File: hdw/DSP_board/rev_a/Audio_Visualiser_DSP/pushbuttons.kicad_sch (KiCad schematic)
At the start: 41 parts, among them J1901 Power Button, J1902 Power, SW1901 Cap_Touch, SW1902 RotaryEncoder_Switch, SW1903 Power, U1901 AT42QT1010-TSHR, U1902 74LVC1G97, U1903 74LVC1G97, U1904 74LVC1G97, U1905 74LVC1G97, U1906 74LVC1G97, U1907 74LVC1G79

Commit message: cleared stale digikey part numbers
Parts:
- C1901, C1903, C1904, C1905, C1906, C1907, C1908, C1909, C1910, C1912, C1913: Digi-Key PN 490-10697-1-ND -> (none)
- C1902: Digi-Key PN 445-12201-1-ND -> (none)
- C1911: Digi-Key PN 490-GRM155R61A106ME11DCT-ND -> (none)
- R1901, R1902: Digi-Key PN RMCF0402FT1K00CT-ND -> (none)
- R1903, R1904, R1906, R1907, R1908, R1909, R1910, R1911, R1912, R1913, R1915, R1916: Digi-Key PN RMCF0402FT10K0CT-ND -> (none)
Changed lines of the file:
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@@
 			)
 		)
-		(property "Digi-Key PN" "490-10697-1-ND"
+		(property "Digi-Key PN" ""
 			(at 55.245 160.02 0)
 			(hide yes)
@@
 			)
 		)
-		(property "Digi-Key PN" "490-GRM155R61A106ME11DCT-ND"
+		(property "Digi-Key PN" ""
 			(at 147.955 36.83 0)
 			(hide yes)
@@
 			)
 		)
-		(property "Digi-Key PN" "RMCF0402FT1K00CT-ND"
+		(property "Digi-Key PN" ""
 			(at 44.45 29.21 0)
 			(hide yes)
@@
 			)
 		)
-		(property "Digi-Key PN" "490-10697-1-ND"
+		(property "Digi-Key PN" ""
 			(at 83.185 74.93 0)
 			(hide yes)
@@
 			)
 		)
-		(property "Digi-Key PN" "490-10697-1-ND"
+		(property "Digi-Key PN" ""
 			(at 83.185 111.76 0)
 			(hide yes)
@@
 			)
 		)
-		(property "Digi-Key PN" "RMCF0402FT1K00CT-ND"
+		(property "Digi-Key PN" ""
 			(at 44.45 34.29 0)
 			(hide yes)
@@
 			)
 		)
-		(property "Digi-Key PN" "490-10697-1-ND"
+		(property "Digi-Key PN" ""
 			(at 103.505 142.24 0)
 			(hide yes)
@@
 			)
 		)
-		(property "Digi-Key PN" "RMCF0402FT10K0CT-ND"
+		(property "Digi-Key PN" ""
 			(at 101.6 64.77 0)
 			(hide yes)
@@
 			)
 		)
-		(property "Digi-Key PN" "490-10697-1-ND"
+		(property "Digi-Key PN" ""
 			(at 159.385 143.51 0)
 			(hide yes)
@@
 			)
 		)
-		(property "Digi-Key PN" "RMCF0402FT10K0CT-ND"
+		(property "Digi-Key PN" ""
 			(at 195.58 139.7 0)
 			(hide yes)
@@
 			)
 		)
-		(property "Digi-Key PN" "490-10697-1-ND"
+		(property "Digi-Key PN" ""
 			(at 103.505 165.1 0)
 			(hide yes)
@@
 			)
 		)
-		(property "Digi-Key PN" "490-10697-1-ND"
+		(property "Digi-Key PN" ""
 			(at 71.755 160.02 0)
 			(hide yes)
@@
 			)
 		)
-		(property "Digi-Key PN" "RMCF0402FT10K0CT-ND"
+		(property "Digi-Key PN" ""
 			(at 130.81 41.91 0)
 			(hide yes)
@@
 			)
 		)
-		(property "Digi-Key PN" "RMCF0402FT10K0CT-ND"
+		(property "Digi-Key PN" ""
 			(at 73.66 127 0)
 			(hide yes)
@@
 			)
 		)
-		(property "Digi-Key PN" "RMCF0402FT10K0CT-ND"
+		(property "Digi-Key PN" ""
 			(at 152.4 114.3 0)
 			(hide yes)
@@
 			)
 		)
-		(property "Digi-Key PN" "RMCF0402FT10K0CT-ND"
+		(property "Digi-Key PN" ""
 			(at 175.26 38.1 0)
 			(hide yes)
@@
 			)
 		)
-		(property "Digi-Key PN" "445-12201-1-ND"
+		(property "Digi-Key PN" ""
 			(at 18.542 163.576 0)
 			(hide yes)
@@
 			)
 		)
-		(property "Digi-Key PN" "490-10697-1-ND"
+		(property "Digi-Key PN" ""
 			(at 120.015 116.84 0)
 			(hide yes)
@@
 			)
 		)
-		(property "Digi-Key PN" "490-10697-1-ND"
+		(property "Digi-Key PN" ""
 			(at 145.415 43.18 0)
 			(hide yes)
@@
 			)
 		)
-		(property "Digi-Key PN" "RMCF0402FT10K0CT-ND"
+		(property "Digi-Key PN" ""
 			(at 135.89 139.7 0)
 			(hide yes)
@@
 			)
 		)
-		(property "Digi-Key PN" "RMCF0402FT10K0CT-ND"
+		(property "Digi-Key PN" ""
 			(at 152.4 77.47 0)
 			(hide yes)
@@
 			)
 		)
-		(property "Digi-Key PN" "490-10697-1-ND"
+		(property "Digi-Key PN" ""
 			(at 120.015 80.01 0)
 			(hide yes)
@@
 			)
 		)
-		(property "Digi-Key PN" "RMCF0402FT10K0CT-ND"
+		(property "Digi-Key PN" ""
 			(at 135.89 162.56 0)
 			(hide yes)
@@
 			)
 		)
-		(property "Digi-Key PN" "RMCF0402FT10K0CT-ND"
+		(property "Digi-Key PN" ""
 			(at 90.17 127 0)
 			(hide yes)
@@
 			)
 		)
-		(property "Digi-Key PN" "RMCF0402FT10K0CT-ND"
+		(property "Digi-Key PN" ""
 			(at 101.6 101.6 0)
 			(hide yes)
@@
 			)
 		)
-		(property "Digi-Key PN" "490-10697-1-ND"
+		(property "Digi-Key PN" ""
 			(at 74.295 44.45 0)
 			(hide yes)
@@
 			)
 		)
-		(property "Digi-Key PN" "RMCF0402FT10K0CT-ND"
+		(property "Digi-Key PN" ""
 			(at 123.19 39.37 0)
 			(hide yes)

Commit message: updated rca jack
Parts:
- J1901: footprint (none) -> Button_Switch_THT:SW_PUSH_6mm
- SW1901: now left out of the parts list
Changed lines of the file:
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@@
 		(body_style 1)
 		(exclude_from_sim yes)
-		(in_bom yes)
+		(in_bom no)
 		(on_board yes)
 		(in_pos_files yes)
@@
 			)
 		)
-		(property "Footprint" ""
+		(property "Footprint" "Button_Switch_THT:SW_PUSH_6mm"
 			(at 38.1 24.13 0)
 			(hide yes)

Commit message: assigned some footprints
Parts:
- U1907: footprint (none) -> Package_TO_SOT_SMD:SOT-363_SC-70-6

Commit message: assigned many digi-key part numbers
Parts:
- C1901, C1903, C1905, C1906: Dielectric X7R -> X7S; Digi-Key PN (none) -> 445-9116-1-ND
- C1902: Dielectric X5R -> X7R; Digi-Key PN (none) -> 490-4516-1-ND
- C1904, C1912: Digi-Key PN (none) -> 490-11917-1-ND
- C1907, C1908, C1909, C1910, C1913: Digi-Key PN (none) -> 1276-CL05B104KB5NNNCCT-ND
- C1911: Digi-Key PN (none) -> 1276-CL05A106MP6NUN8CT-ND
- J1902: Digi-Key PN (none) -> 277-1247-ND
- R1901, R1902: Digi-Key PN (none) -> 311-1.00KLRCT-ND
- R1903, R1904, R1906, R1907, R1908, R1909, R1910, R1911, R1912, R1913, R1915, R1916: Digi-Key PN (none) -> 311-10.0KLRCT-ND
- R1905, R1914: Digi-Key PN (none) -> 311-0.0LRCT-ND
- SW1903: footprint (none) -> Button_Switch_THT:SW_PUSH_6mm; Digi-Key PN (none) -> 450-1650-ND
- U1907: footprint Package_TO_SOT_SMD:SOT-363_SC-70-6 -> Package_TO_SOT_SMD:SOT-353_SC-70-5; Digi-Key PN (none) -> 296-9850-1-ND
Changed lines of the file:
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@@
 			)
 		)
-		(property "Digi-Key PN" ""
+		(property "Digi-Key PN" "445-9116-1-ND"
 			(at 55.245 160.02 0)
 			(hide yes)
@@
 			)
 		)
-		(property "Dielectric" "X7R"
+		(property "Dielectric" "X7S"
 			(at 69.85 175.26 0)
 			(show_name no)
@@
 			)
 		)
-		(property "Digi-Key PN" ""
+		(property "Digi-Key PN" "1276-CL05A106MP6NUN8CT-ND"
 			(at 147.955 36.83 0)
 			(hide yes)
@@
 			)
 		)
-		(property "Digi-Key PN" ""
+		(property "Digi-Key PN" "311-1.00KLRCT-ND"
 			(at 44.45 29.21 0)
 			(hide yes)
@@
 			)
 		)
-		(property "Digi-Key PN" ""
+		(property "Digi-Key PN" "445-9116-1-ND"
 			(at 83.185 74.93 0)
 			(hide yes)
@@
 			)
 		)
-		(property "Dielectric" "X7R"
+		(property "Dielectric" "X7S"
 			(at 97.79 90.17 0)
 			(show_name no)
@@
 			)
 		)
-		(property "Digi-Key PN" ""
+		(property "Digi-Key PN" "445-9116-1-ND"
 			(at 83.185 111.76 0)
 			(hide yes)
@@
 			)
 		)
-		(property "Dielectric" "X7R"
+		(property "Dielectric" "X7S"
 			(at 97.79 127 0)
 			(show_name no)
@@
 			)
 		)
-		(property "Digi-Key PN" ""
+		(property "Digi-Key PN" "311-1.00KLRCT-ND"
 			(at 44.45 34.29 0)
 			(hide yes)
@@
 			)
 		)
-		(property "Digi-Key PN" ""
+		(property "Digi-Key PN" "1276-CL05B104KB5NNNCCT-ND"
 			(at 103.505 142.24 0)
 			(hide yes)
@@
 			)
 		)
-		(property "Digi-Key PN" ""
+		(property "Digi-Key PN" "311-10.0KLRCT-ND"
 			(at 101.6 64.77 0)
 			(hide yes)
@@
 			)
 		)
-		(property "Digi-Key PN" ""
+		(property "Digi-Key PN" "1276-CL05B104KB5NNNCCT-ND"
 			(at 159.385 143.51 0)
 			(hide yes)
@@
 			)
 		)
-		(property "Digi-Key PN" ""
+		(property "Digi-Key PN" "311-10.0KLRCT-ND"
 			(at 195.58 139.7 0)
 			(hide yes)
@@
 			)
 		)
-		(property "Digi-Key PN" ""
+		(property "Digi-Key PN" "1276-CL05B104KB5NNNCCT-ND"
 			(at 103.505 165.1 0)
 			(hide yes)
@@
 			)
 		)
-		(property "Digi-Key PN" ""
+		(property "Digi-Key PN" "445-9116-1-ND"
 			(at 71.755 160.02 0)
 			(hide yes)
@@
 			)
 		)
-		(property "Dielectric" "X7R"
+		(property "Dielectric" "X7S"
 			(at 86.36 175.26 0)
 			(show_name no)
@@
 			)
 		)
-		(property "Digi-Key PN" ""
+		(property "Digi-Key PN" "311-10.0KLRCT-ND"
 			(at 130.81 41.91 0)
 			(hide yes)
@@
 			)
 		)
-		(property "Digi-Key PN" ""
+		(property "Digi-Key PN" "311-10.0KLRCT-ND"
 			(at 73.66 127 0)
 			(hide yes)
@@
 			)
 		)
-		(property "Digi-Key PN" ""
+		(property "Digi-Key PN" "311-0.0LRCT-ND"
 			(at 83.82 16.51 0)
 			(hide yes)
@@
 			)
 		)
-		(property "Footprint" ""
+		(property "Footprint" "Button_Switch_THT:SW_PUSH_6mm"
 			(at 72.39 88.9 0)
 			(hide yes)
@@
 			)
 		)
+		(property "Digi-Key PN" "450-1650-ND"
+			(at 77.47 88.9 0)
+			(hide yes)
+			(show_name no)
+			(do_not_autoplace no)
+			(effects
+				(font
+					(size 1.27 1.27)
+				)
+			)
+		)
 		(pin "1"
 		)
@@
 			)
 		)
-		(property "Digi-Key PN" ""
+		(property "Digi-Key PN" "311-10.0KLRCT-ND"
 			(at 152.4 114.3 0)
 			(hide yes)
@@
 			)
 		)
-		(property "Digi-Key PN" ""
+		(property "Digi-Key PN" "311-10.0KLRCT-ND"
 			(at 175.26 38.1 0)
 			(hide yes)
@@
 			)
 		)
-		(property "Digi-Key PN" ""
+		(property "Digi-Key PN" "490-4516-1-ND"
 			(at 18.542 163.576 0)
 			(hide yes)
@@
 			)
 		)
-		(property "Dielectric" "X5R"
+		(property "Dielectric" "X7R"
 			(at 74.93 45.974 90)
 			(show_name no)
@@
 			)
 		)
-		(property "Digi-Key PN" ""
+		(property "Digi-Key PN" "1276-CL05B104KB5NNNCCT-ND"
 			(at 120.015 116.84 0)
 			(hide yes)
@@
 			)
 		)
-		(property "Digi-Key PN" ""
+		(property "Digi-Key PN" "490-11917-1-ND"
 			(at 145.415 43.18 0)
 			(hide yes)
@@
 			)
 		)
+		(property "Digi-Key PN" "277-1247-ND"
+			(at 38.1 81.28 0)
+			(hide yes)
+			(show_name no)
+			(do_not_autoplace no)
+			(effects
+				(font
+					(size 1.27 1.27)
+				)
+			)
+		)
 		(pin "1"
 		)
@@
 			)
 		)
-		(property "Digi-Key PN" ""
+		(property "Digi-Key PN" "311-10.0KLRCT-ND"
 			(at 135.89 139.7 0)
 			(hide yes)
@@
 			)
 		)
-		(property "Digi-Key PN" ""
+		(property "Digi-Key PN" "311-10.0KLRCT-ND"
 			(at 152.4 77.47 0)
 			(hide yes)
@@
 			)
 		)
-		(property "Digi-Key PN" ""
+		(property "Digi-Key PN" "311-0.0LRCT-ND"
 			(at 147.32 73.66 0)
 			(hide yes)
@@
 			)
 		)
-		(property "Digi-Key PN" ""
+		(property "Digi-Key PN" "1276-CL05B104KB5NNNCCT-ND"
 			(at 120.015 80.01 0)
 			(hide yes)
@@
 			)
 		)
-		(property "Digi-Key PN" ""
+		(property "Digi-Key PN" "311-10.0KLRCT-ND"
 			(at 135.89 162.56 0)
 			(hide yes)
@@
 			)
 		)
-		(property "Footprint" "Package_TO_SOT_SMD:SOT-363_SC-70-6"
+		(property "Footprint" "Package_TO_SOT_SMD:SOT-353_SC-70-5"
 			(at 158.75 146.05 0)
 			(hide yes)
@@
 			)
 		)
+		(property "Digi-Key PN" "296-9850-1-ND"
+			(at 158.75 146.05 0)
+			(hide yes)
+			(show_name no)
+			(do_not_autoplace no)
+			(effects
+				(font
+					(size 1.27 1.27)
+				)
+			)
+		)
 		(pin "3"
 		)
@@
 			)
 		)
-		(property "Digi-Key PN" ""
+		(property "Digi-Key PN" "311-10.0KLRCT-ND"
 			(at 90.17 127 0)
 			(hide yes)
@@
 			)
 		)
-		(property "Digi-Key PN" ""
+		(property "Digi-Key PN" "311-10.0KLRCT-ND"
 			(at 101.6 101.6 0)
 			(hide yes)
@@
 			)
 		)
-		(property "Digi-Key PN" ""
+		(property "Digi-Key PN" "490-11917-1-ND"
 			(at 74.295 44.45 0)
 			(hide yes)
@@
 			)
 		)
-		(property "Digi-Key PN" ""
+		(property "Digi-Key PN" "311-10.0KLRCT-ND"
 			(at 123.19 39.37 0)
 			(hide yes)

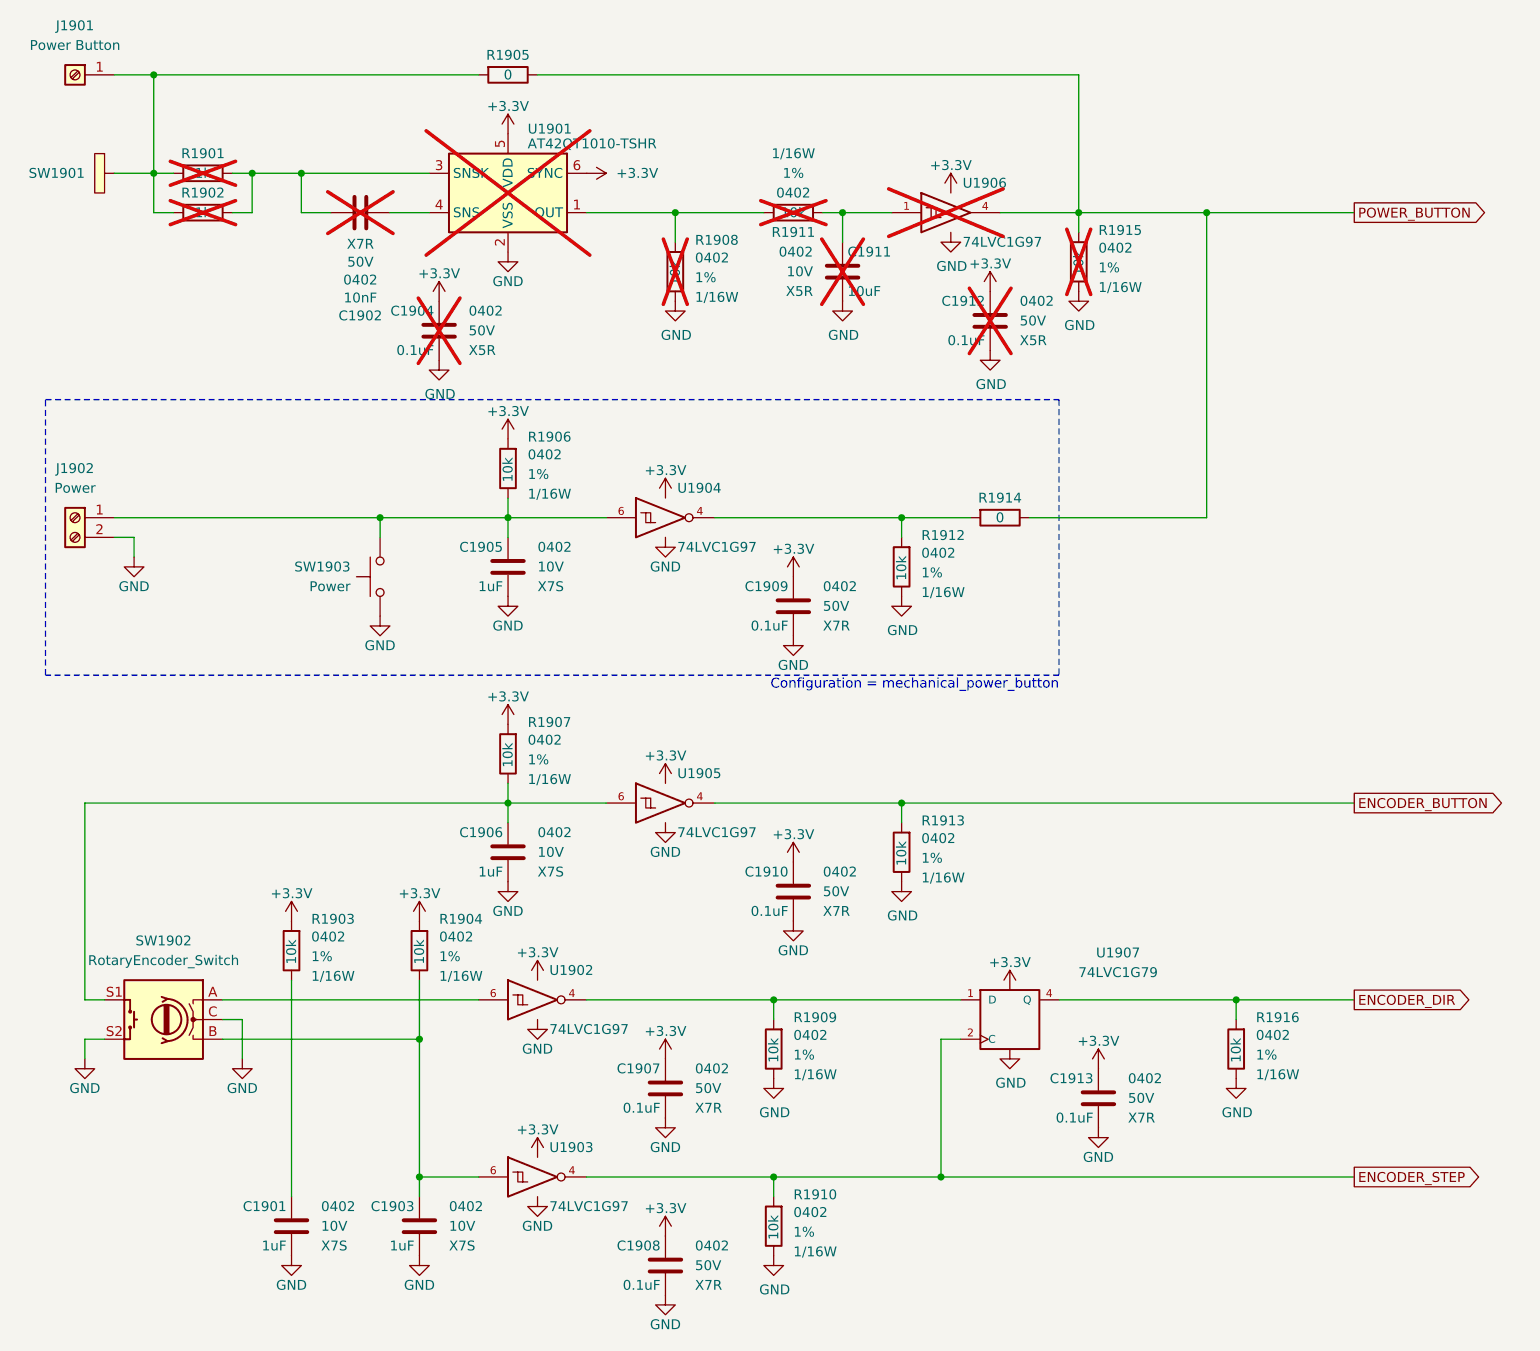
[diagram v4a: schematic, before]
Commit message: Added a bunch of stuff to the schematic
Moved to adafruit I2C rotary encoder module. Added signal test points. Added some design schematic notes. Added LEd output connector ESD diodes. Consolidated on a single schottky diode. Connected most signals to MCU
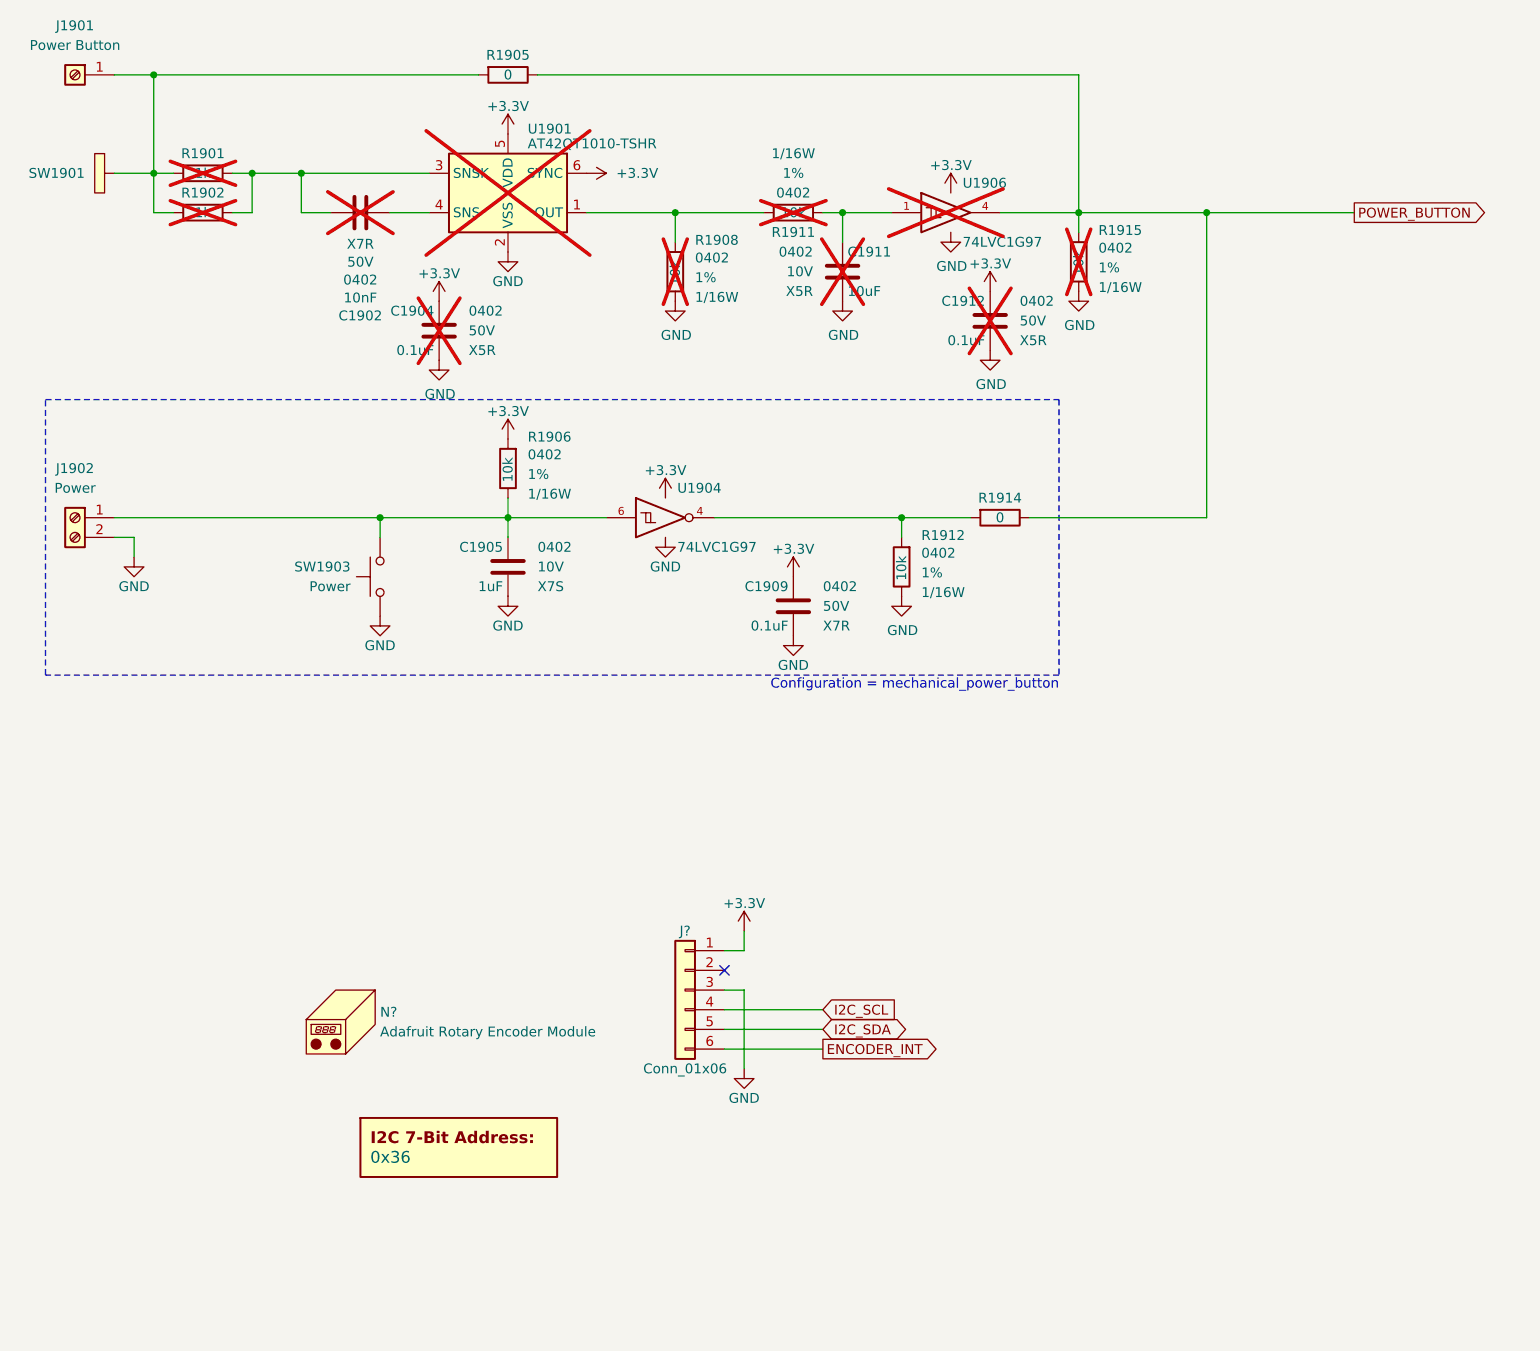
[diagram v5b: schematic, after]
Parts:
- removed C1901, C1903, C1906: 1uF, Capacitors_SMD:C_0402, symbol Custom_Library:C_Custom
- removed C1907, C1908, C1910, C1913: 0.1uF, Capacitors_SMD:C_0402, symbol Custom_Library:C_Custom
- removed R1903, R1904, R1907, R1909, R1910, R1913, R1916: 10k, Resistors_SMD:R_0402, symbol Custom_Library:R_Custom
- removed SW1902: RotaryEncoder_Switch, symbol Device:RotaryEncoder_Switch
- removed U1902, U1903, U1905: 74LVC1G97, Package_TO_SOT_SMD:SOT-363_SC-70-6, symbol Custom Library:74LVC1G97_Power_NOT
- removed U1907: 74LVC1G79, Package_TO_SOT_SMD:SOT-353_SC-70-5, symbol Custom Library:74LVC1G79_Power
- added DOC?: 0x36, symbol Custom Library:I2C_Address
- added J?: Conn_01x06, symbol Connector_Generic:Conn_01x06
- added N?: Adafruit Rotary Encoder Module, symbol Mechanical:Housing
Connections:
- net +3.3V: now also J?.1 (Pin_1)
- net GND: now also J?.3 (Pin_3)
- new net ENCODER_INT: J?.6 (Pin_6)
- new net I2C_SCL: J?.4 (Pin_4)
- new net I2C_SDA: J?.5 (Pin_5)
- no-connect marks 0 -> 1

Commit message: Added simulation outputs, sim readme
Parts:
- gave numbers to parts that had none: 3
- renumbered C1902 to C1901, C1904 to C1902, C1905 to C1903, C1909 to C1904, C1911 to C1905, C1912 to C1906, R1905 to R1903, R1906 to R1904, R1908 to R1905, R1911 to R1906, R1912 to R1907, R1914 to R1908, R1915 to R1909, SW1903 to SW1902, U1904 to U1902, U1906 to U1903

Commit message: Defined legit KiCad BOM variants
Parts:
- removed J1901: Power Button, Button_Switch_THT:SW_PUSH_6mm, symbol Connector:Screw_Terminal_01x01
- added J1901: Power, TerminalBlock_Phoenix:TerminalBlock_Phoenix_MKDS-1,5-2-5.08_1x02_P5.08mm_Horizontal, symbol Connector:Screw_Terminal_01x02
- R1903: now not fitted
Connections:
- net at R1901.1, R1902.1, R1903.1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: now also J1901.1 (Pin_1), J1901.2 (Pin_2)

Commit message: Add audio signal path test points, fix development variant excludes
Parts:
- J1901: now not fitted
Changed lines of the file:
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@@
 		(on_board yes)
 		(in_pos_files yes)
-		(dnp no)
+		(dnp yes)
 		(fields_autoplaced yes)
 		(property "Reference" "J1901"
@@
 					(variant
 						(name "Default")
+						(dnp no)
 					)
 					(variant
 						(name "Development")
+						(dnp no)
 					)
 				)
